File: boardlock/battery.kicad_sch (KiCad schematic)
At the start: 20 parts, among them J1 Conn_01x02, J2 Conn_01x02, U4 BQ27441DRZR-G1A, U5 BQ24075RGT

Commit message: buck-boost WIP
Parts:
- R20, R21, R22, R23: footprint Resistor_SMD:R_0805_2012Metric_Pad1.20x1.40mm_HandSolder -> Resistor_SMD:R_0603_1608Metric_Pad0.98x0.95mm_HandSolder
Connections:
- net ISET: now reaches R23.1, U5.16 (ISET)
- net TIMER: now reaches R20.1, U5.14 (TMR)
- net N_Charge_EN: now reaches R21.1, U5.4 (~{CE})
- net ILIM: now reaches R22.1, U5.12 (ILIM)
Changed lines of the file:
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@@
     (effects (font (size 1.27 1.27)) (justify left bottom))
+  )
+  (label "N_Charge_EN" (at 110.49 83.82 0) (fields_autoplaced)
+    (effects (font (size 1.27 1.27)) (justify left bottom))
+  )
+  (label "TIMER" (at 110.49 86.36 0) (fields_autoplaced)
+    (effects (font (size 1.27 1.27)) (justify left bottom))
+  )
+  (label "ILIM" (at 69.85 83.82 180) (fields_autoplaced)
+    (effects (font (size 1.27 1.27)) (justify right bottom))
+  )
+  (label "ISET" (at 76.2 86.36 180) (fields_autoplaced)
+    (effects (font (size 1.27 1.27)) (justify right bottom))
   )
   (global_label "BATT_CHARGE_VOUT" (shape output) (at 60.96 168.91 0) (fields_autoplaced)
@@
       (effects (font (size 1.27 1.27)) (justify left))
     )
-    (property "Footprint" "Resistor_SMD:R_0805_2012Metric_Pad1.20x1.40mm_HandSolder" (at 77.216 92.964 90)
+    (property "Footprint" "Resistor_SMD:R_0603_1608Metric_Pad0.98x0.95mm_HandSolder" (at 77.216 92.964 90)
       (effects (font (size 1.27 1.27)) hide)
     )
@@
       (effects (font (size 1.27 1.27)) (justify left))
     )
-    (property "Footprint" "Resistor_SMD:R_0805_2012Metric_Pad1.20x1.40mm_HandSolder" (at 111.506 91.694 90)
+    (property "Footprint" "Resistor_SMD:R_0603_1608Metric_Pad0.98x0.95mm_HandSolder" (at 111.506 91.694 90)
       (effects (font (size 1.27 1.27)) hide)
     )
@@
       (effects (font (size 1.27 1.27)) (justify left))
     )
-    (property "Footprint" "Resistor_SMD:R_0805_2012Metric_Pad1.20x1.40mm_HandSolder" (at 122.936 91.694 90)
+    (property "Footprint" "Resistor_SMD:R_0603_1608Metric_Pad0.98x0.95mm_HandSolder" (at 122.936 91.694 90)
       (effects (font (size 1.27 1.27)) hide)
     )
@@
       (effects (font (size 1.27 1.27)) (justify left))
     )
-    (property "Footprint" "Resistor_SMD:R_0805_2012Metric_Pad1.20x1.40mm_HandSolder" (at 67.056 92.964 90)
-      (effects (font (size 1.27 1.27)) hide)
-    )
+    (property "Footprint" "Resistor_SMD:R_0603_1608Metric_Pad0.98x0.95mm_HandSolder" (at 67.056 92.964 90)
+      (effects (font (size 1.27 1.27)) hide)
+    )

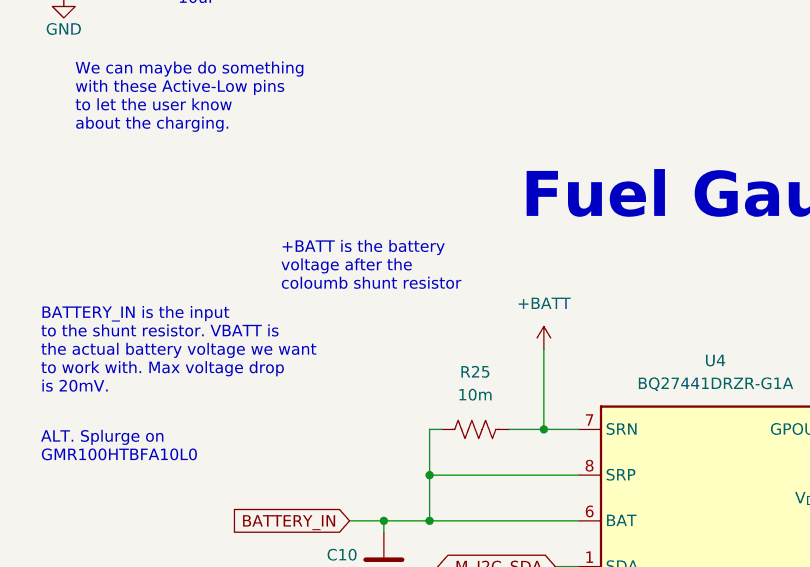
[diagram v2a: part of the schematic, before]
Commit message: spelling error
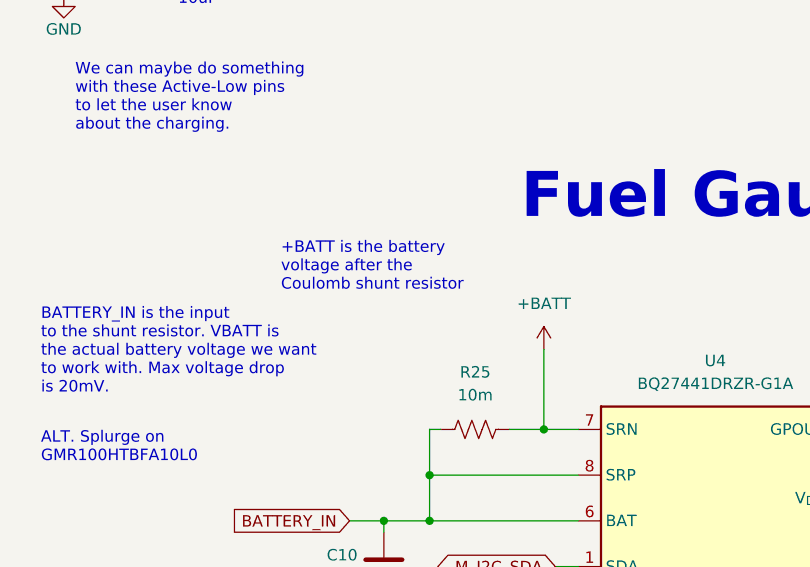
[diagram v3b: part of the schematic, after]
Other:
- note added: "+BATT is the battery voltage after the Coulomb shunt resistor"
- note removed: "+BATT is the battery voltage after the coloumb shunt resistor"
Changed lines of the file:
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@@
     (effects (font (size 5 5) (thickness 1) bold) (justify left bottom))
   )
-  (text "+BATT is the battery\nvoltage after the\ncoloumb shunt resistor"
+  (text "+BATT is the battery\nvoltage after the\nCoulomb shunt resistor"
     (at 167.64 110.49 0)
     (effects (font (size 1.27 1.27)) (justify left bottom))
